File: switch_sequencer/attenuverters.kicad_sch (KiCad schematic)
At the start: 0 parts

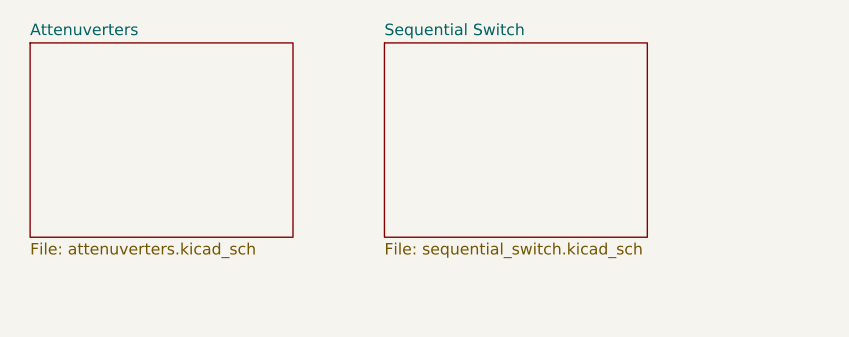
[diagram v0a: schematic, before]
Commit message: more switch sequencer
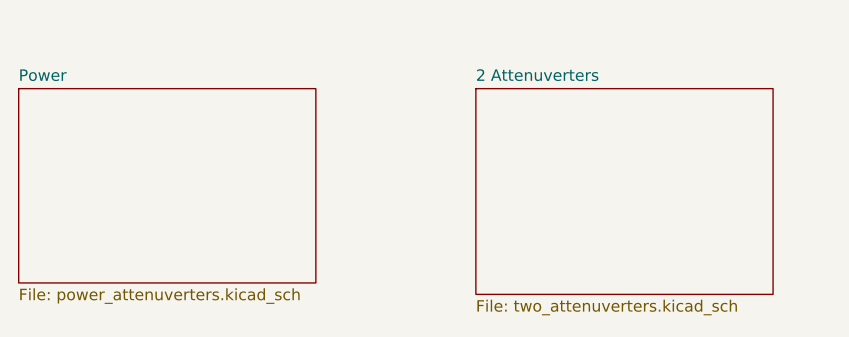
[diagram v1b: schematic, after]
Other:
- removed sheet Attenuverters
- removed sheet Sequential Switch
- added sheet 2 Attenuverters (two_attenuverters.kicad_sch)
- added sheet Power (power_attenuverters.kicad_sch)
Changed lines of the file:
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@@
 	(paper "A4")
 	(sheet
-		(at 96.52 62.23)
-		(size 29.21 21.59)
+		(at 55.88 67.31)
+		(size 33.02 21.59)
 		(fields_autoplaced yes)
 		(stroke
@@
 			(color 0 0 0 0.0000)
 		)
-		(property "Sheetname" "Sequential Switch"
-			(at 96.52 61.5184 0)
+		(property "Sheetname" "Power"
+			(at 55.88 66.5984 0)
 			(effects
 				(font
@@
 			)
 		)
-		(property "Sheetfile" "sequential_switch.kicad_sch"
-			(at 96.52 84.4046 0)
+		(property "Sheetfile" "power_attenuverters.kicad_sch"
+			(at 55.88 89.4846 0)
 			(effects
 				(font
@@
 		(instances
 			(project "switch_sequencer"
-				(path "/1090b42d-0526-4901-ae26-1a4493d10820"
-					(page "3")
+				(path "/1090b42d-0526-4901-ae26-1a4493d10820/c21975fb-1aad-4817-bd76-de40397c1585"
+					(page "6")
 				)
 			)
@@
 	)
 	(sheet
-		(at 57.15 62.23)
-		(size 29.21 21.59)
+		(at 106.68 67.31)
+		(size 33.02 22.86)
 		(fields_autoplaced yes)
 		(stroke
@@
 			(color 0 0 0 0.0000)
 		)
-		(property "Sheetname" "Attenuverters"
-			(at 57.15 61.5184 0)
+		(property "Sheetname" "2 Attenuverters"
+			(at 106.68 66.5984 0)
 			(effects
 				(font
@@
 			)
 		)
-		(property "Sheetfile" "attenuverters.kicad_sch"
-			(at 57.15 84.4046 0)
+		(property "Sheetfile" "two_attenuverters.kicad_sch"
+			(at 106.68 90.7546 0)
 			(effects
 				(font
@@
 		(instances
 			(project "switch_sequencer"
-				(path "/1090b42d-0526-4901-ae26-1a4493d10820"
-					(page "2")
+				(path "/1090b42d-0526-4901-ae26-1a4493d10820/c21975fb-1aad-4817-bd76-de40397c1585"
+					(page "7")
 				)
 			)
 		)
 	)
-	(sheet_instances
-		(path "/"
-			(page "1")
-		)
-	)
